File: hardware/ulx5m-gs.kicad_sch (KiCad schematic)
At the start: 4 parts

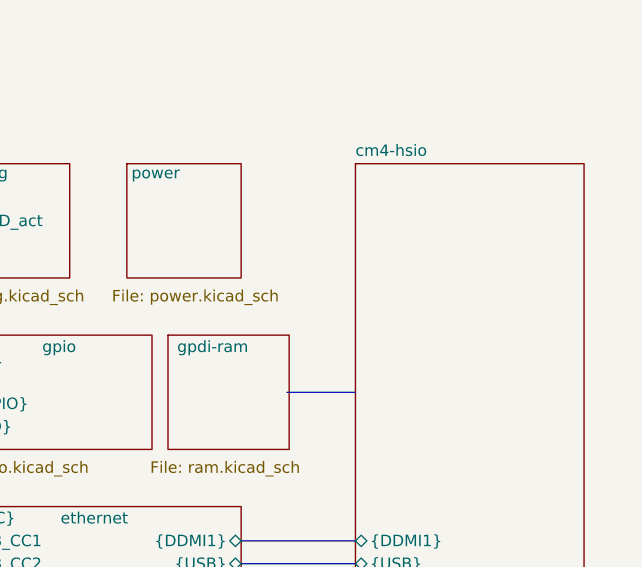
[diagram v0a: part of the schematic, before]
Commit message: GPIO are now routed differential
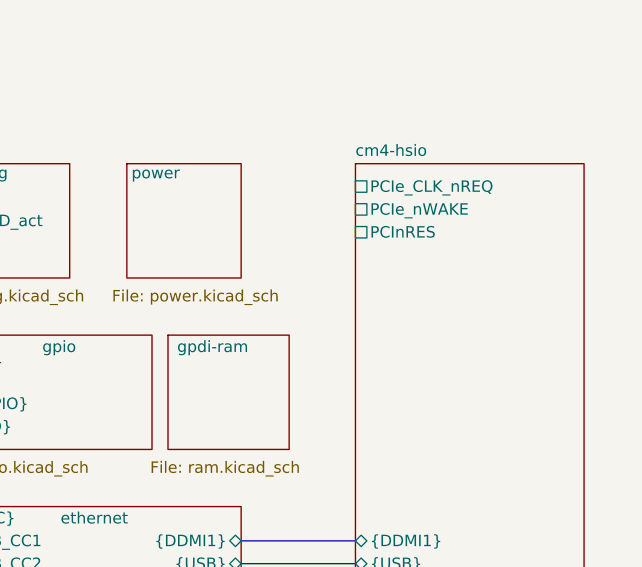
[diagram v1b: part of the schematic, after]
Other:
- sheet cm4-hsio ports: added PCIe_CLK_nREQ, PCIe_nWAKE, PCInRES; removed none
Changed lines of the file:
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@@
-		)
-	)
-	(bus
-		(pts
-			(xy 95.25 64.77) (xy 102.87 64.77)
-		)
-		(stroke
-			(width 0)
-			(type default)
 		)
 	)
@@
 			(effects
 				(font
+					(size 1.27 1.27)
+				)
+				(justify left)
+			)
+		)
+		(pin "PCIe_CLK_nREQ" passive
+			(at 102.87 41.91 180)
+			(effects
+				(font
+					(size 1.27 1.27)
+				)
+				(justify left)
+			)
+		)
+		(pin "PCIe_nWAKE" passive
+			(at 102.87 44.45 180)
+			(effects
+				(font
+					(size 1.27 1.27)
+				)
+				(justify left)
+			)
+		)
+		(pin "PCInRES" passive
+			(at 102.87 46.99 180)
+			(effects
+				(font

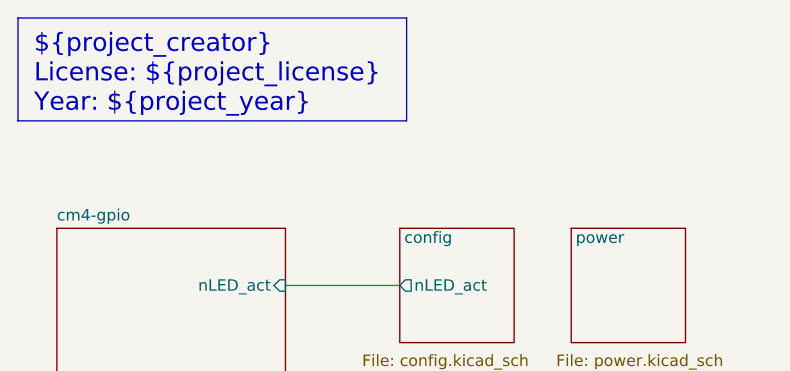
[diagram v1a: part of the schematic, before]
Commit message: Switching A and B on TXS0202YZPR adding pass resistors
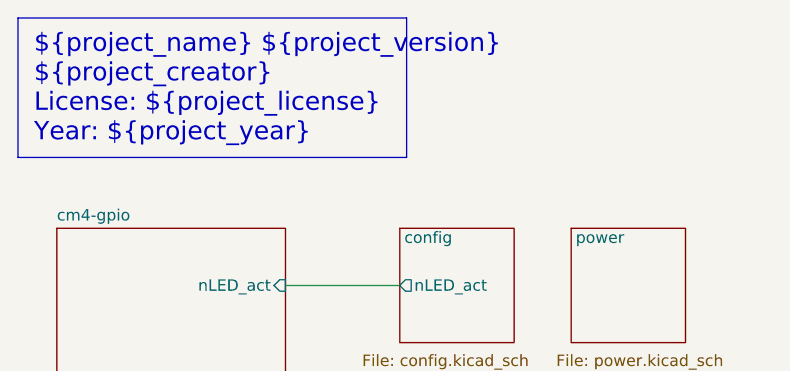
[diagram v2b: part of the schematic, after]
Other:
- note added: "${project_name} ${project_version} ${project_creator} License: ${project_license} Year: ${project_year}"
- note removed: "${project_creator} License: ${project_license} Year: ${project_year}"
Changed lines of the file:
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@@
 	(rectangle
 		(start 16.002 16.002)
-		(end 59.182 27.432)
+		(end 59.182 31.496)
 		(stroke
 			(width 0)
@@
 		)
 	)
-	(text "${project_creator}\nLicense: ${project_license}\nYear: ${project_year}"
+	(text "${project_name} ${project_version}\n${project_creator}\nLicense: ${project_license}\nYear: ${project_year}"
 		(exclude_from_sim no)
 		(at 17.78 17.78 0)

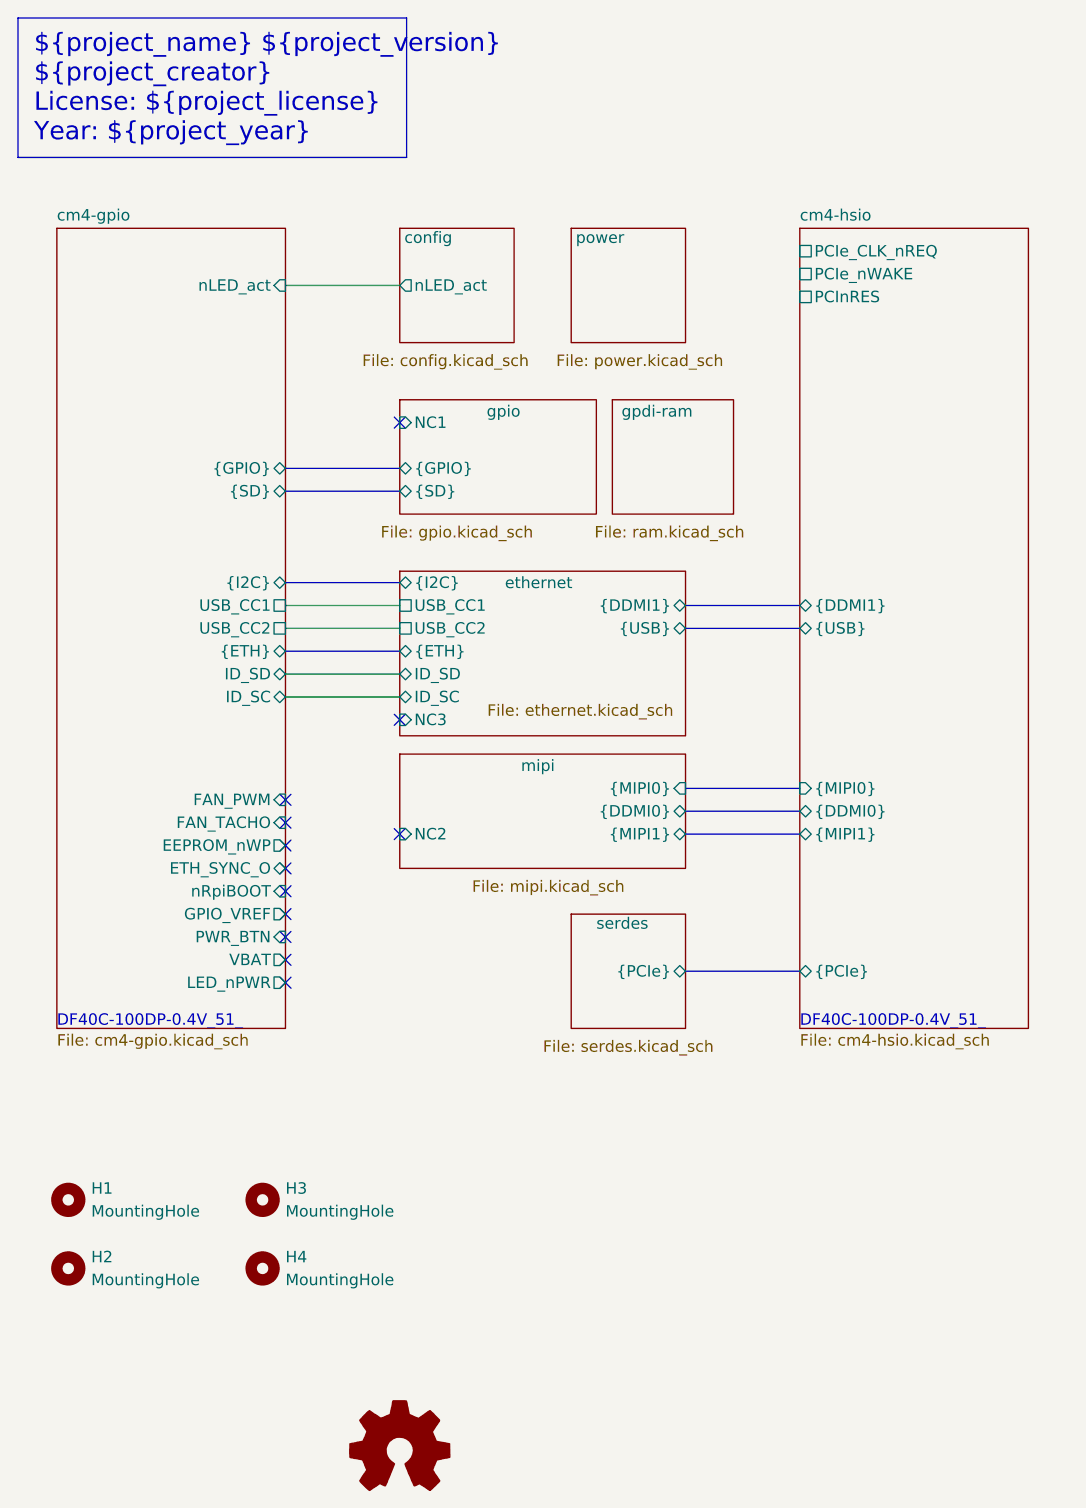
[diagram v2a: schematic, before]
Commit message: Connecting PWR and FAN_PWM to NC pins, using NC3 for Ethernet clock
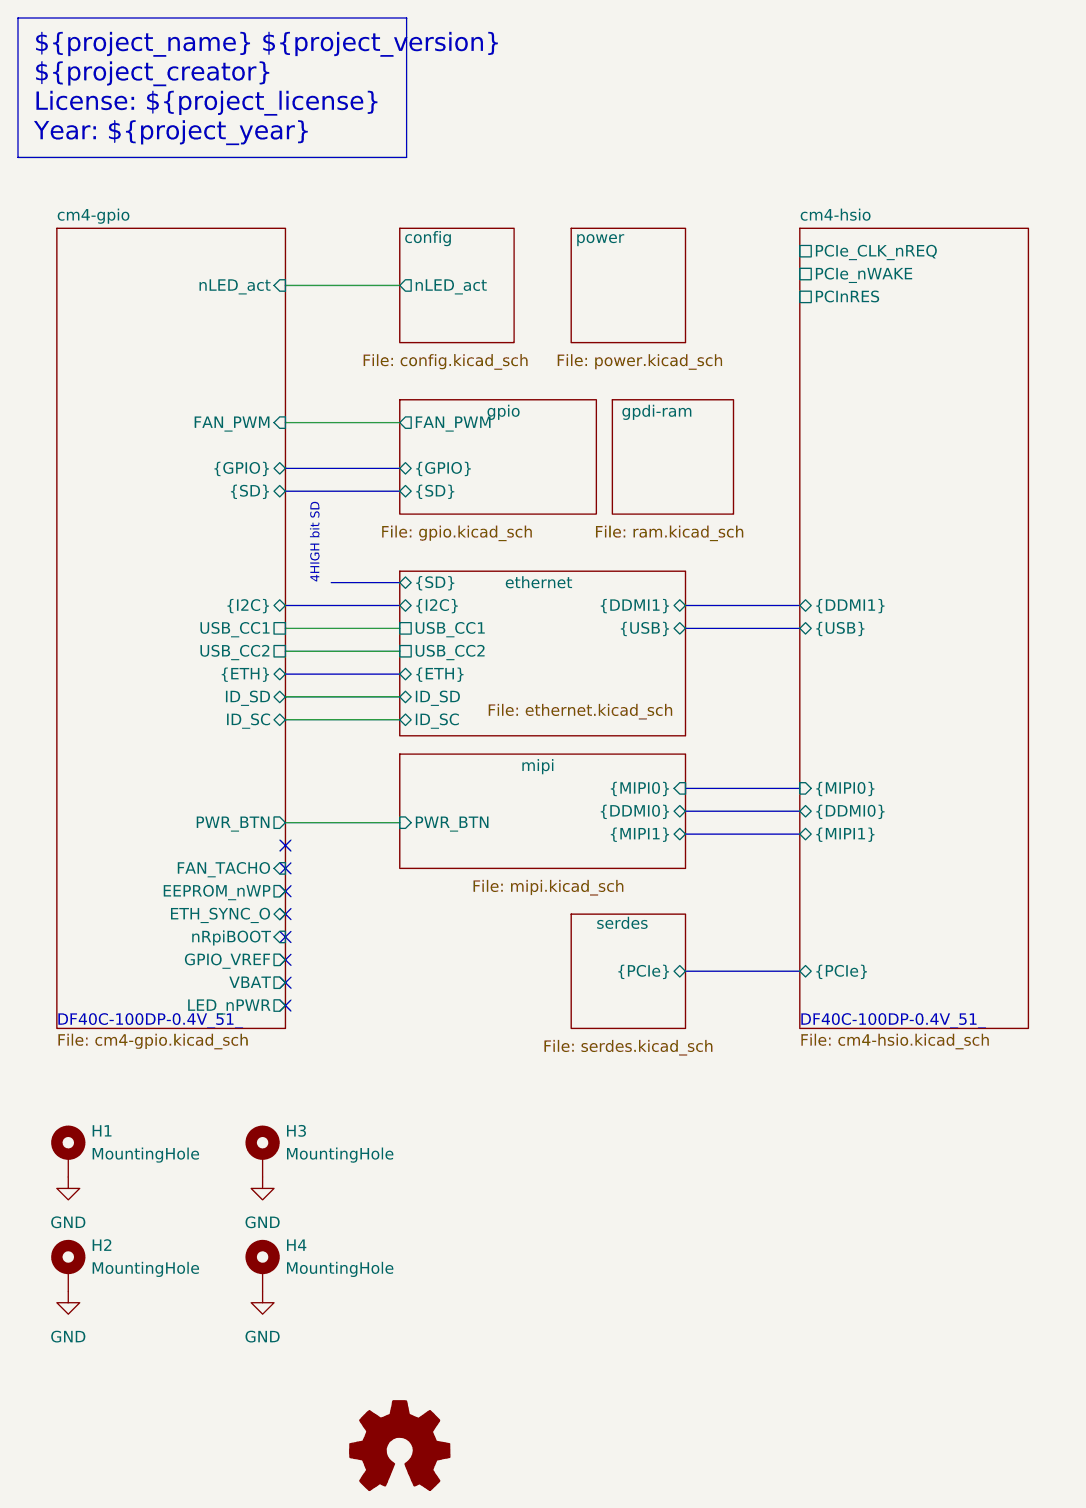
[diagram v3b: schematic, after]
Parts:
- H1, H2, H3, H4: footprint MountingHole:MountingHole_2.7mm_M2.5 -> MountingHole:MountingHole_2.7mm_M2.5_DIN965_Pad; symbol Mechanical:MountingHole -> Mechanical:MountingHole_Pad; now left out of the parts list
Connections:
- new net GND: H1.1, H2.1, H3.1, H4.1
- no-connect marks 12 -> 8
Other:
- sheet ethernet ports: added {SD}; removed NC3
- sheet gpio ports: added FAN_PWM; removed NC1
- sheet mipi ports: added PWR_BTN; removed NC2
- note added: "4HIGH bit SD"

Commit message: Updating sch - moving power select resistors to bottom
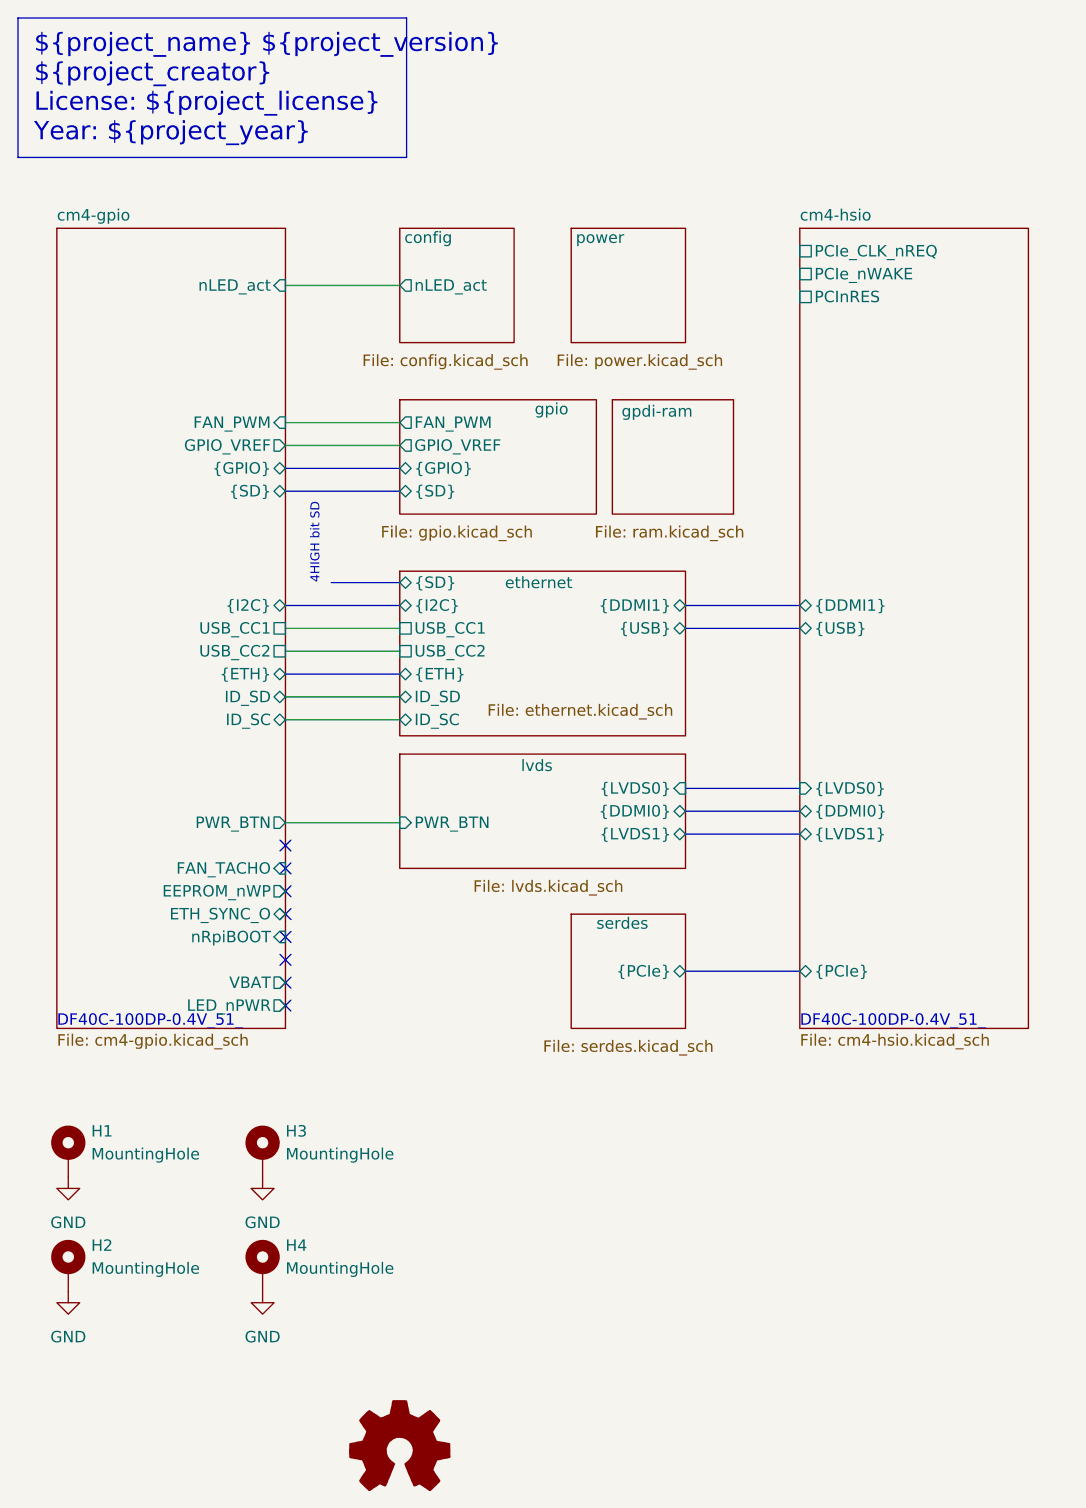
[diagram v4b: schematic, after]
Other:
- sheet mipi renamed lvds
- sheet cm4-hsio ports: added {LVDS0}, {LVDS1}; removed {MIPI0}, {MIPI1}
- sheet gpio ports: added GPIO_VREF; removed none
- sheet lvds: file mipi.kicad_sch -> lvds.kicad_sch
- sheet lvds ports: added {LVDS0}, {LVDS1}; removed {MIPI0}, {MIPI1}
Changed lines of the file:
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@@
+		)
+	)
+	(wire
+		(pts
+			(xy 45.72 63.5) (xy 58.42 63.5)
+		)
+		(stroke
+			(width 0)
+			(type default)
 		)
 	)
@@
 		)
 		(pin "GPIO_VREF" output
-			(at 45.72 120.65 0)
+			(at 45.72 63.5 0)
 			(effects
 				(font
@@
 		)
 		(property "Sheetname" "gpio"
-			(at 68.072 60.452 0)
+			(at 73.406 60.198 0)
 			(effects
 				(font
@@
 		(pin "FAN_PWM" output
 			(at 58.42 60.96 180)
+			(effects
+				(font
+					(size 1.27 1.27)
+				)
+				(justify left)
+			)
+		)
+		(pin "GPIO_VREF" output
+			(at 58.42 63.5 180)
 			(effects
 				(font
@@
 			(color 0 0 0 0.0000)
 		)
-		(property "Sheetname" "mipi"
+		(property "Sheetname" "lvds"
 			(at 71.882 99.822 0)
 			(effects
@@
 			)
 		)
-		(property "Sheetfile" "mipi.kicad_sch"
+		(property "Sheetfile" "lvds.kicad_sch"
 			(at 74.93 111.76 0)
 			(effects
@@
 			)
 		)
-		(pin "{MIPI1}" bidirectional
+		(pin "{LVDS0}" input
+			(at 90.17 101.6 0)
+			(effects
+				(font
+					(size 1.27 1.27)
+				)
+				(justify right)
+			)
+		)
+		(pin "{LVDS1}" bidirectional
 			(at 90.17 106.68 0)
-			(effects
-				(font
-					(size 1.27 1.27)
-				)
-				(justify right)
-			)
-		)
-		(pin "{MIPI0}" input
-			(at 90.17 101.6 0)
 			(effects
 				(font
@@
 			)
 		)
-		(pin "{MIPI1}" bidirectional
-			(at 102.87 106.68 180)
-			(effects
-				(font
-					(size 1.27 1.27)
-				)
-				(justify left)
-			)
-		)
-		(pin "{MIPI0}" input
-			(at 102.87 101.6 180)
-			(effects
-				(font
-					(size 1.27 1.27)
-				)
-				(justify left)
-			)
-		)
 		(pin "PCIe_CLK_nREQ" passive
 			(at 102.87 41.91 180)
@@
 			(effects
 				(font
+					(size 1.27 1.27)
+				)
+				(justify left)
+			)
+		)
+		(pin "{LVDS0}" input
+			(at 102.87 101.6 180)
+			(effects
+				(font
+					(size 1.27 1.27)
+				)
+				(justify left)
+			)
+		)
+		(pin "{LVDS1}" bidirectional
+			(at 102.87 106.68 180)
+			(effects
+				(font
